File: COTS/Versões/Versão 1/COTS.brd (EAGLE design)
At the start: 76.2 x 79.7 mm, 10 parts

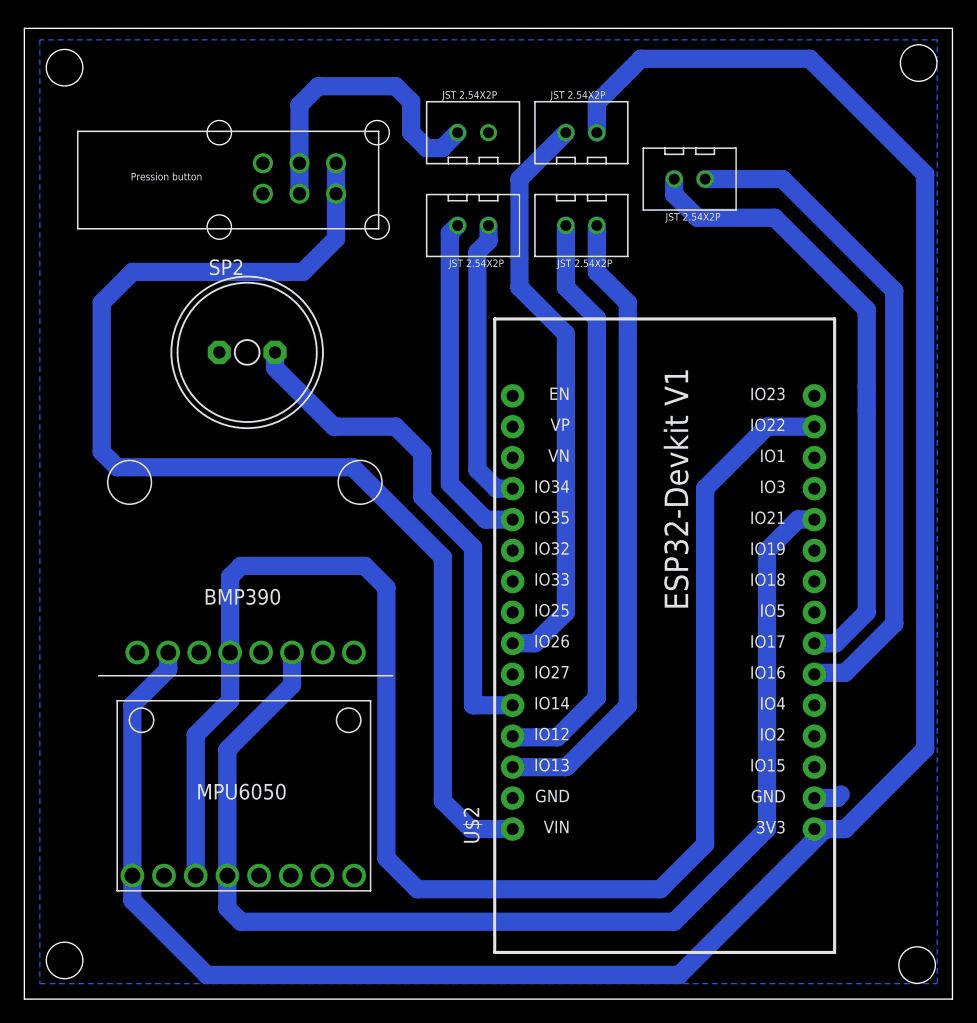
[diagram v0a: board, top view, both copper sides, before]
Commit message: CHORE: adicionando modelos 3D
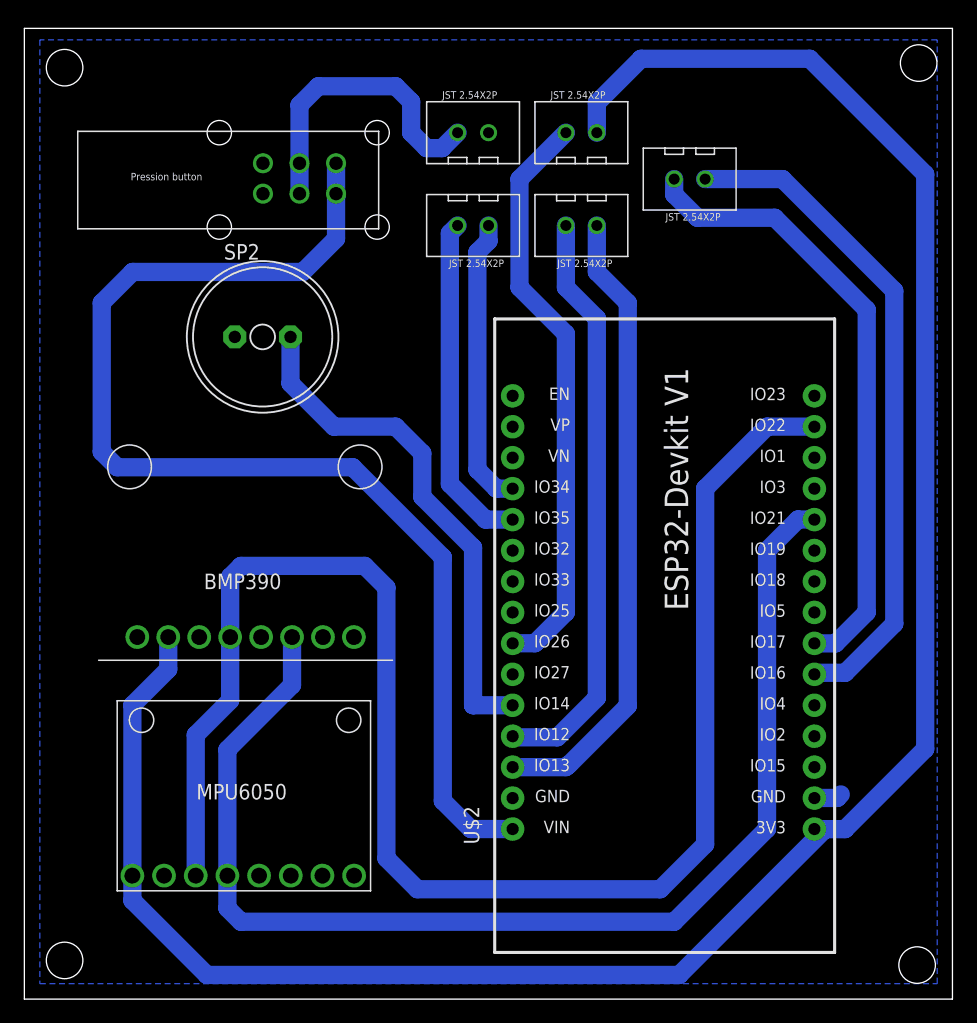
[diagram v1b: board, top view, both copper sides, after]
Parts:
- moved SP2 1.80 mm to (19.6, 54.4)
- moved U$3 1.27 mm to (17.8, 38.1)
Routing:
- net SDA: track 98.9 -> 100.2 mm
- net 3V3: track 179.7 -> 181.0 mm
- net BUZZER: track 41.9 -> 42.7 mm

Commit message: FEAT: adicionando regulador de tensao 5V
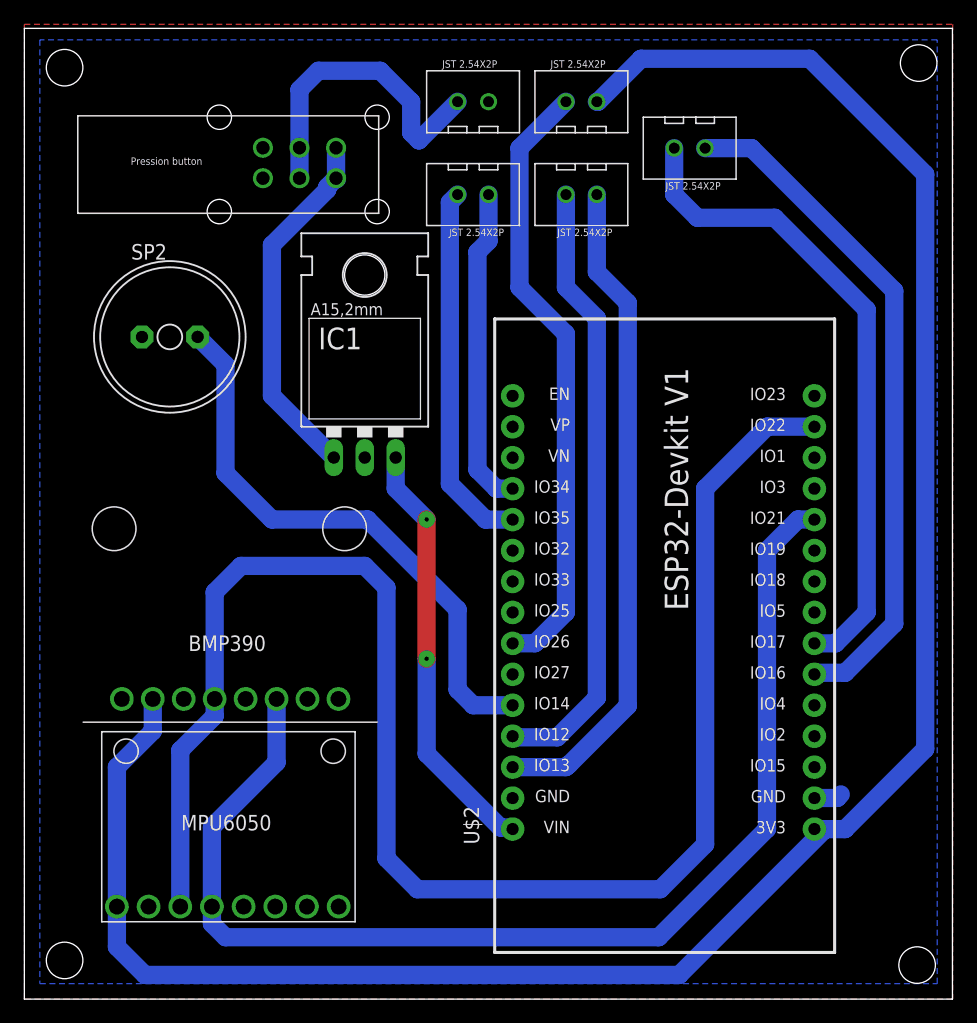
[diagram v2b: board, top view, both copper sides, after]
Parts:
- added IC1: (no value), v-reg:78XXL
- moved SP2 7.62 mm to (11.9, 54.4)
- moved U$3 5.24 mm to (16.5, 33.0)
- moved U$1 2.84 mm to (16.5, 17.8)
- moved U$4 2.54 mm to (45.7, 66.0)
- moved U$9 2.54 mm to (36.8, 66.0)
- moved U$5 2.54 mm to (45.7, 73.7)
- moved U$6 2.54 mm to (36.8, 73.7)
- moved U$7 2.54 mm to (54.6, 69.8)
- moved U$10 1.27 mm to (17.8, 68.6)
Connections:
- new net 5V: IC1.OUT, U$2.30
- net GND: now also IC1.GND
- net VIN: now also IC1.IN; no longer U$2.30
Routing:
- net VIN: track 98.2 -> 29.8 mm
- net 5V: track 0.00 -> 35.0 mm, vias 0 -> 2
- net BUZZER: track 42.7 -> 47.4 mm
- net 3V3: track 181.0 -> 176.9 mm
- net SCL: track 130.9 -> 134.0 mm
- net SKIB2: track 48.4 -> 50.9 mm
- net SKIB1: track 52.0 -> 54.6 mm
- net OPTOACOPLADOR2: track 27.8 -> 30.4 mm
- net OPTOACOPLADOR1: track 24.0 -> 26.5 mm
- net SIGNAL1: track 48.0 -> 50.5 mm
- net TX2: track 51.2 -> 53.7 mm
- net SDA: track 100.2 -> 98.2 mm
- net RX2: track 54.9 -> 56.0 mm
- net V_BATTERY: track 25.0 -> 26.1 mm
- added copper zone on layer 1, net GND

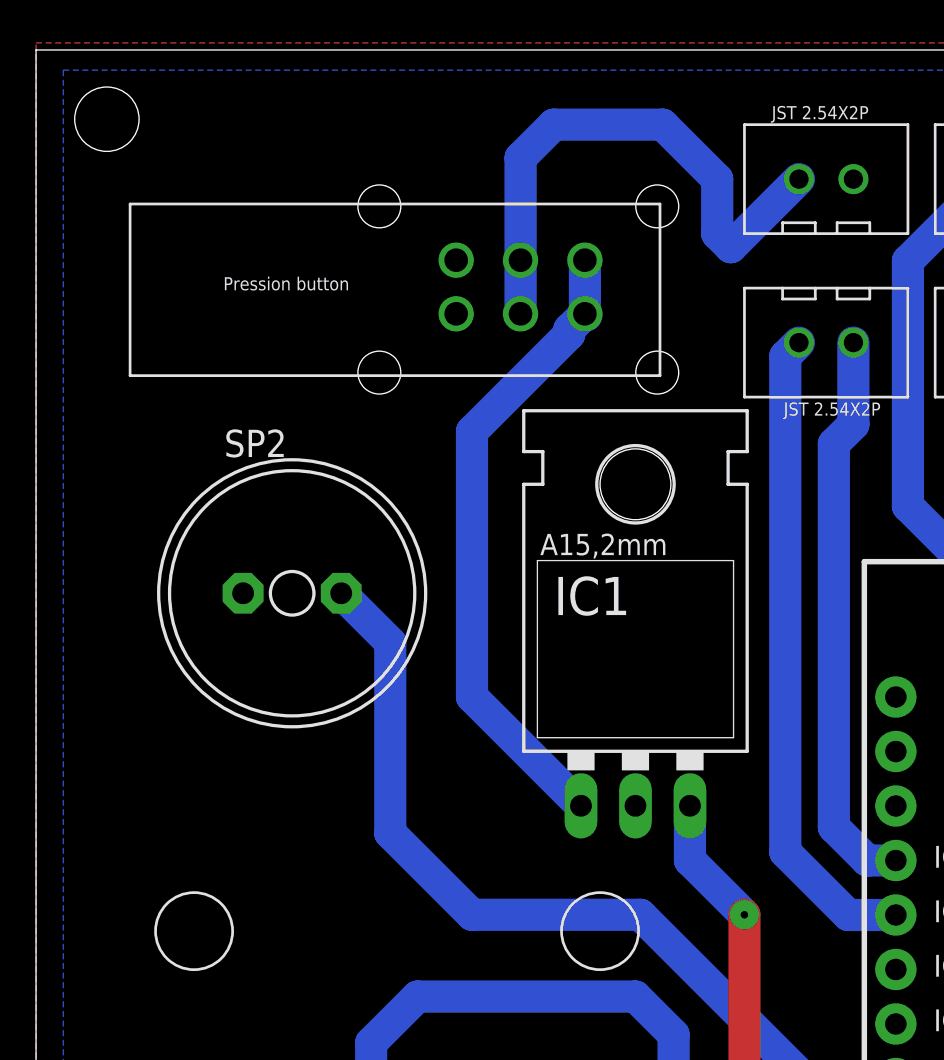
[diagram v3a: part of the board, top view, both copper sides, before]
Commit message: FIX: consertando chave de acionamento
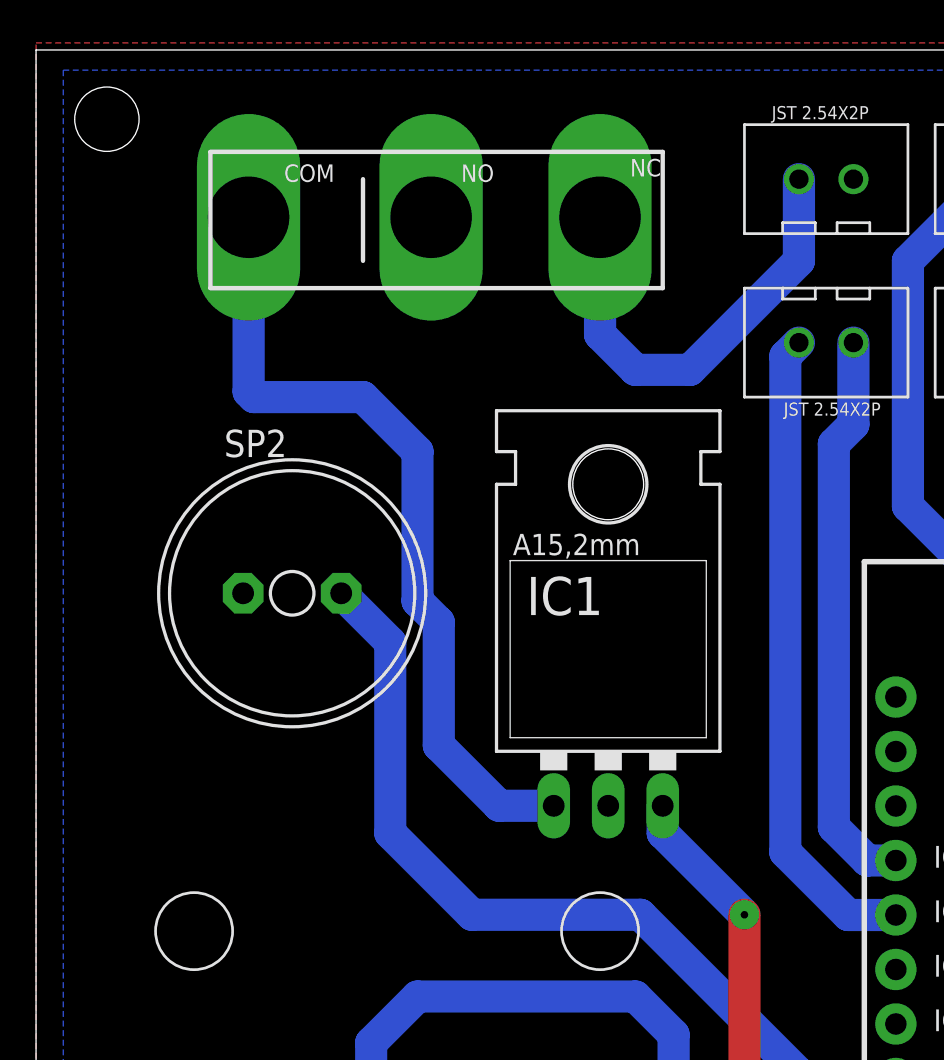
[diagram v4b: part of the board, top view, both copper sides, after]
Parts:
- removed U$10: PRESSION_BUTTON, CRD:PRESSION_BUTTON_FOOTPRINT
- added U$8: CHAVE_SS-5GL, CRD:CHAVESS-5GL
- moved IC1 1.27 mm to (26.7, 48.3)
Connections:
- net VIN: now also U$8.P$1; no longer U$10.PL1, U$10.PR1
- net V_BATTERY: now also U$8.P$3; no longer U$10.PL2, U$10.PR2
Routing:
- net VIN: track 29.8 -> 37.8 mm
- net V_BATTERY: track 26.1 -> 21.3 mm
- net 5V: track 35.0 -> 35.5 mm
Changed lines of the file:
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@@
 </layers>
 <board>
-<fusionsync huburn="a.YnVzaW5lc3M6ZGlzY2VudGUxNzg" projecturn="a.YnVzaW5lc3M6ZGlzY2VudGUxNzgjRDIwMjIwNjExNTMyNjQzNTAx" f3durn="urn:adsk.wipprod:dm.lineage:ibykAXc8Rg2DjItFZulgfg" pcbguid="" lastpulledtime="2025-09-05T22:45:31Z" lastsyncedchangeguid="" latestrevisionid="e6b1c730-9f95-4a30-b171-4c3269d38a0a" lastsyncedrevisionid="33f84b92-60a2-4bf8-9c50-a51f5ebe0a74" lastboardhashguid="b32a0115-e0c3-fe5a-bab1-fdc4e4641bb9" lastpushedtime="2024-04-21T15:54:42Z" linktopcb3d="true"/>
+<fusionsync huburn="a.YnVzaW5lc3M6ZGlzY2VudGUxMTk5" projecturn="a.YnVzaW5lc3M6ZGlzY2VudGUxMTk5IzIwMjUwNjA1OTM2MzUyODI2" f3durn="urn:adsk.wipprod:dm.lineage:mIVt_tiyTuWaVOghQ5xvIA" pcbguid="" lastpulledtime="" lastsyncedchangeguid="" latestrevisionid="0f4c0286-4885-44cf-a761-73f221ec9438" lastsyncedrevisionid="0f4c0286-4885-44cf-a761-73f221ec9438" lastboardhashguid="76bae40b-276a-4a11-8513-12fb5d83ee83" lastpushedtime="2025-09-08T04:59:23Z" linktopcb3d="false"/>
 <plain>
 <dimension x1="-3.81" y1="0" x2="-3.81" y2="79.629" x3="-7.62" y3="39.8145" textsize="1.778" layer="47"/>
@@
 <element name="U$7" library="CRD" library_urn="urn:adsk.eagle:library:39051337" package="JST2.54X2P_FOOTPRINT" package3d_urn="urn:adsk.eagle:package:39191967/2" value="JST2.54X2P" x="54.61" y="69.85" smashed="yes" rot="R180"/>
 <element name="U$9" library="CRD" library_urn="urn:adsk.eagle:library:39051337" package="JST2.54X2P_FOOTPRINT" package3d_urn="urn:adsk.eagle:package:39191967/2" value="JST2.54X2P" x="36.83" y="66.04" smashed="yes" rot="R180"/>
-<element name="U$10" library="CRD" library_urn="urn:adsk.eagle:library:39051337" package="PRESSION_BUTTON_FOOTPRINT" package3d_urn="urn:adsk.eagle:package:43483815/3" override_package3d_urn="urn:adsk.eagle:package:49474180/2" override_package_urn="urn:adsk.eagle:footprint:43483813/3" value="PRESSION_BUTTON" x="17.78" y="68.58" smashed="yes" rot="R180"/>
-<element name="SP2" library="buzzer" library_urn="urn:adsk.eagle:library:113" package="AL11P" package3d_urn="urn:adsk.eagle:package:5308/1" override_package3d_urn="urn:adsk.eagle:package:49473303/2" override_package_urn="urn:adsk.eagle:footprint:5250/1" value="AL11P" x="11.938" y="54.356" smashed="yes">
+<element name="SP2" library="buzzer" library_urn="urn:adsk.eagle:library:113" package="AL11P" package3d_urn="urn:adsk.eagle:package:5308/1" override_package3d_urn="urn:adsk.eagle:package:49481862/2" override_package_urn="urn:adsk.eagle:footprint:5250/1" value="AL11P" x="11.938" y="54.356" smashed="yes">
 <attribute name="MF" value="" x="11.938" y="54.356" size="1.778" layer="27" display="off"/>
 <attribute name="MPN" value="" x="11.938" y="54.356" size="1.778" layer="27" display="off"/>
@@
 <attribute name="VALUE" x="8.128" y="51.181" size="1.27" layer="27" ratio="10"/>
 </element>
-<element name="IC1" library="v-reg" library_urn="urn:adsk.eagle:library:409" package="78XXL" package3d_urn="urn:adsk.eagle:package:30361/1" override_package3d_urn="urn:adsk.eagle:package:49478860/2" override_package_urn="urn:adsk.eagle:footprint:30303/1" value="" x="27.94" y="48.26" smashed="yes">
-<attribute name="NAME" x="24.13" y="53.34" size="1.778" layer="25" ratio="10"/>
-<attribute name="POPULARITY" value="10" x="27.94" y="48.26" size="1.778" layer="27" display="off"/>
-<attribute name="VALUE" x="24.003" y="50.8" size="1.778" layer="27" ratio="10"/>
+<element name="IC1" library="v-reg" library_urn="urn:adsk.eagle:library:409" package="78XXL" package3d_urn="urn:adsk.eagle:package:30361/1" override_package3d_urn="urn:adsk.eagle:package:49481863/2" override_package_urn="urn:adsk.eagle:footprint:30303/1" value="" x="26.67" y="48.26" smashed="yes">
+<attribute name="NAME" x="22.86" y="53.34" size="1.778" layer="25" ratio="10"/>
+<attribute name="POPULARITY" value="10" x="26.67" y="48.26" size="1.778" layer="27" display="off"/>
+<attribute name="VALUE" x="22.733" y="50.8" size="1.778" layer="27" ratio="10"/>
 </element>
+<element name="U$8" library="CRD" library_urn="urn:adsk.eagle:library:39051337" package="CHAVESS-5GL" package3d_urn="urn:adsk.eagle:package:45208058/14" value="CHAVE_SS-5GL" x="19.05" y="71.12" smashed="yes"/>
 </elements>
 <signals>
 <signal name="VIN">
-<contactref element="U$10" pad="PL1"/>
-<contactref element="U$10" pad="PR1"/>
-<wire x1="25.583" y1="67.382" x2="25.654" y2="67.311" width="1.5" layer="16"/>
-<wire x1="25.583" y1="67.382" x2="25.583" y2="69.882" width="1.5" layer="16"/>
 <contactref element="IC1" pad="IN"/>
-<wire x1="25.583" y1="67.382" x2="24.858" y2="66.657" width="1.5" layer="16"/>
-<wire x1="24.858" y1="66.657" x2="24.858" y2="66.4396625" width="1.5" layer="16"/>
-<wire x1="24.858" y1="66.4396625" x2="20.32" y2="61.9016625" width="1.5" layer="16"/>
-<wire x1="20.32" y1="49.53" x2="25.4" y2="44.45" width="1.5" layer="16"/>
-<wire x1="20.32" y1="61.9016625" x2="20.32" y2="49.53" width="1.5" layer="16"/>
+<contactref element="U$8" pad="P$1"/>
+<wire x1="24.13" y1="44.45" x2="21.59" y2="44.45" width="1.5" layer="16"/>
+<wire x1="18.772" y1="47.268" x2="18.772" y2="53.00695625" width="1.5" layer="16"/>
+<wire x1="18.772" y1="53.00695625" x2="17.78" y2="53.99895625" width="1.5" layer="16"/>
+<wire x1="17.78" y1="53.99895625" x2="17.78" y2="60.96" width="1.5" layer="16"/>
+<wire x1="17.78" y1="60.96" x2="15.24" y2="63.5" width="1.5" layer="16"/>
+<wire x1="15.24" y1="63.5" x2="10.16" y2="63.5" width="1.5" layer="16"/>
+<wire x1="10.16" y1="63.5" x2="9.906" y2="63.754" width="1.5" layer="16"/>
+<wire x1="9.906" y1="63.754" x2="9.906" y2="71.882" width="1.5" layer="16"/>
+<wire x1="21.59" y1="44.45" x2="18.772" y2="47.268" width="1.5" layer="16"/>
 </signal>
 <signal name="GND">
@@
 <signal name="V_BATTERY">
 <contactref element="U$6" pad="1"/>
-<contactref element="U$10" pad="PL2"/>
-<contactref element="U$10" pad="PR2"/>
-<wire x1="32.385" y1="70.485" x2="31.75" y2="71.12" width="1.5" layer="16"/>
-<wire x1="31.75" y1="73.66" x2="29.21" y2="76.2" width="1.5" layer="16"/>
-<wire x1="29.21" y1="76.2" x2="24.13" y2="76.2" width="1.5" layer="16"/>
-<wire x1="22.583" y1="74.653" x2="22.583" y2="69.882" width="1.5" layer="16"/>
-<wire x1="35.56" y1="73.66" x2="32.385" y2="70.485" width="1.5" layer="16"/>
-<wire x1="31.75" y1="71.12" x2="31.75" y2="73.66" width="1.5" layer="16"/>
-<wire x1="24.13" y1="76.2" x2="22.583" y2="74.653" width="1.5" layer="16"/>
-<wire x1="22.583" y1="69.882" x2="22.583" y2="67.382" width="1.5" layer="16"/>
+<wire x1="35.56" y1="73.66" x2="35.56" y2="69.85" width="1.5" layer="16"/>
+<contactref element="U$8" pad="P$3"/>
+<wire x1="35.56" y1="69.85" x2="30.48" y2="64.77" width="1.5" layer="16"/>
+<wire x1="26.289" y1="68.961" x2="26.289" y2="69.85" width="1.5" layer="16"/>
+<wire x1="26.289" y1="69.85" x2="26.289" y2="71.882" width="1.5" layer="16"/>
+<wire x1="30.48" y1="64.77" x2="27.94" y2="64.77" width="1.5" layer="16"/>
+<wire x1="27.94" y1="64.77" x2="26.289" y2="66.421" width="1.5" layer="16"/>
+<wire x1="26.289" y1="66.421" x2="26.289" y2="68.961" width="1.5" layer="16"/>
 </signal>
 <signal name="RX2">
@@
 <wire x1="33.02" y1="27.94" x2="33.02" y2="39.37" width="1.5" layer="1"/>
 <via x="33.02" y="39.37" extent="1-16" drill="0.35"/>
-<wire x1="33.02" y1="39.37" x2="30.48" y2="41.91" width="1.5" layer="16"/>
-<wire x1="30.48" y1="41.91" x2="30.48" y2="44.45" width="1.5" layer="16"/>
+<wire x1="33.02" y1="39.37" x2="29.21" y2="43.18" width="1.5" layer="16"/>
+<wire x1="29.21" y1="43.18" x2="29.21" y2="44.45" width="1.5" layer="16"/>
 </signal>
 </signals>

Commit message: atualização placas
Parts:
- added U$10: BMP280V1, CRD:BMP280_FOOTPRINT
- moved IC1 4.02 mm to (25.4, 52.1)
- moved U$3 4.02 mm to (17.8, 36.8)
- moved U$1 2.84 mm to (17.8, 15.2), turned to 270 degrees
- moved U$4 1.27 mm to (45.7, 64.8)
- moved U$9 1.27 mm to (36.8, 64.8)
- moved U$8 1.27 mm to (19.1, 72.4)
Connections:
- net 3V3: now also U$10.VCC
- net GND: now also U$10.GND; no longer U$2.2
- net SCL: now also U$10.SCL
- net SDA: now also U$10.SDA
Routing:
- net SDA: track 98.2 -> 128.6 mm
- net 3V3: track 176.9 -> 205.2 mm
- net SCL: track 134.0 -> 157.6 mm
- net V_BATTERY: track 21.3 -> 9.48 mm
- net VIN: track 37.8 -> 32.6 mm
- net GND: track 2.29 -> 6.73 mm, vias 0 -> 2
- net 5V: track 35.5 -> 39.8 mm
- net SKIB2: track 50.9 -> 49.6 mm
- net SKIB1: track 54.6 -> 53.3 mm
- net OPTOACOPLADOR1: track 26.5 -> 25.2 mm
- net OPTOACOPLADOR2: track 30.4 -> 29.1 mm
- net BUZZER: track 47.4 -> 46.7 mm
- removed copper zone on layer 1, net GND
